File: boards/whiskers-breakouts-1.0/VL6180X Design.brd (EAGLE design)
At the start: 76.5 x 21 mm, 19 parts, among them J2 6-PIN_2MM-V, Q3 BSS138, Q4 BSS138, U1 VL6180X, U2 MIC5225_2.8V, U3 VL6180X, U4 VL6180X

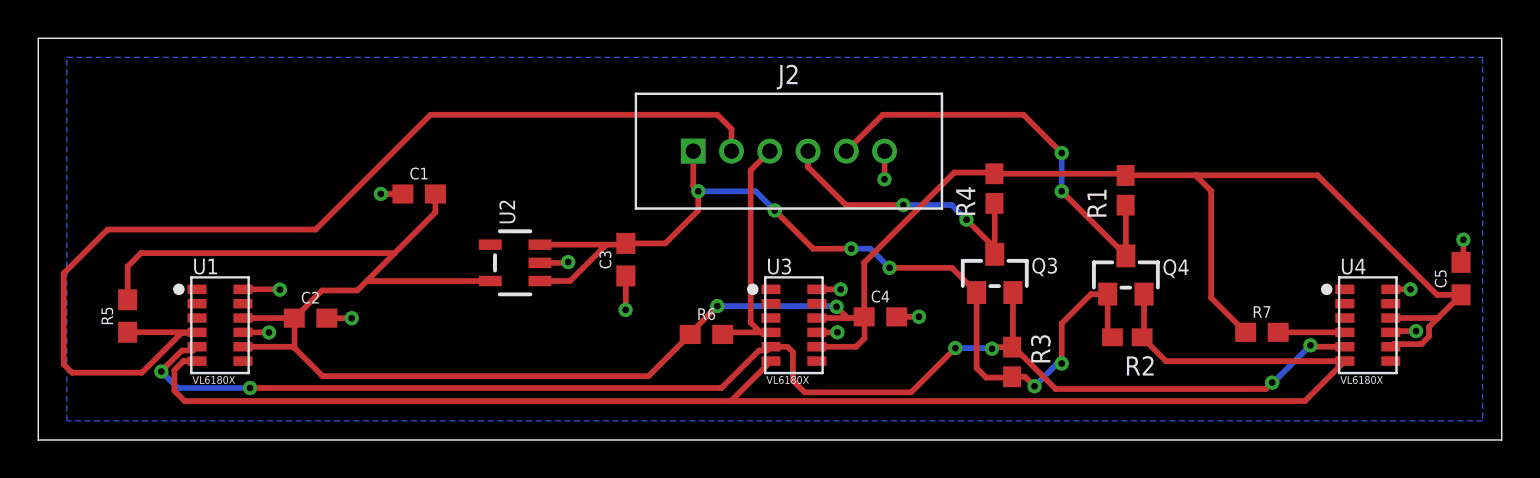
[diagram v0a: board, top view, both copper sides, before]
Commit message: Update VL6180X Design.brd
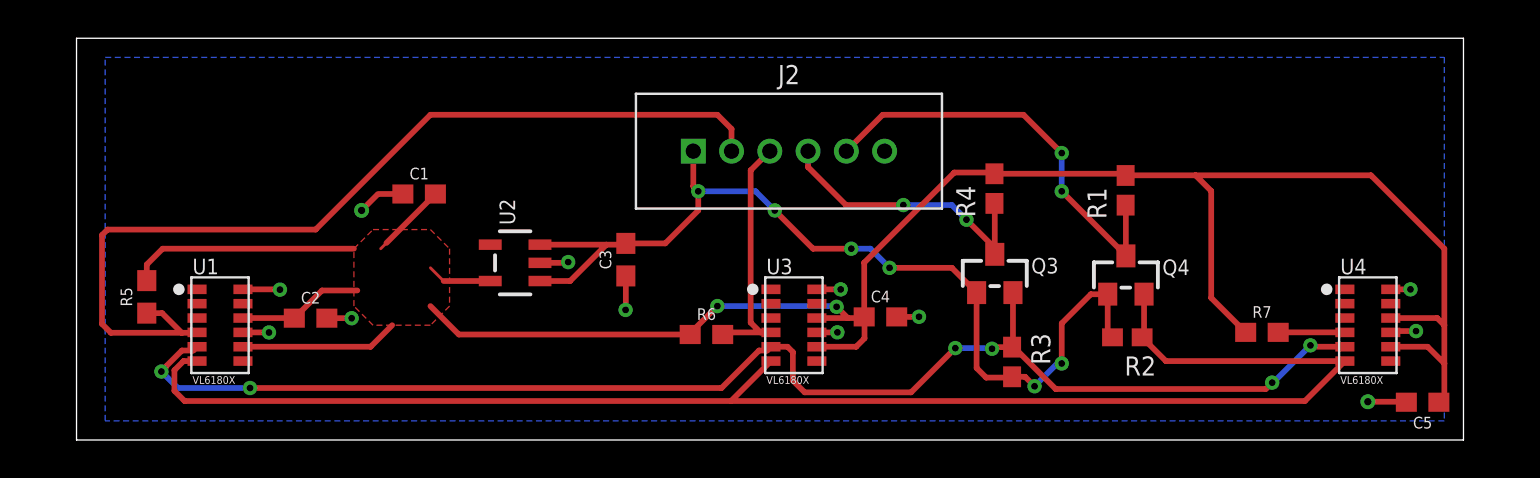
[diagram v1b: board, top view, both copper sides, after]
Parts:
- moved C5 6.77 mm to (72.9, 16.0), turned to 180 degrees
- moved R5 1.41 mm to (6.17, 21.5)
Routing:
- net VCC: track 133.2 -> 124.3 mm
- net RST_1: track 56.2 -> 49.0 mm
- net GND: track 17.6 -> 18.3 mm, vias 13 -> 12
- added copper zone on layer 1, net VCC
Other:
- board size 76.5 x 21 mm -> 72.5 x 21 mm

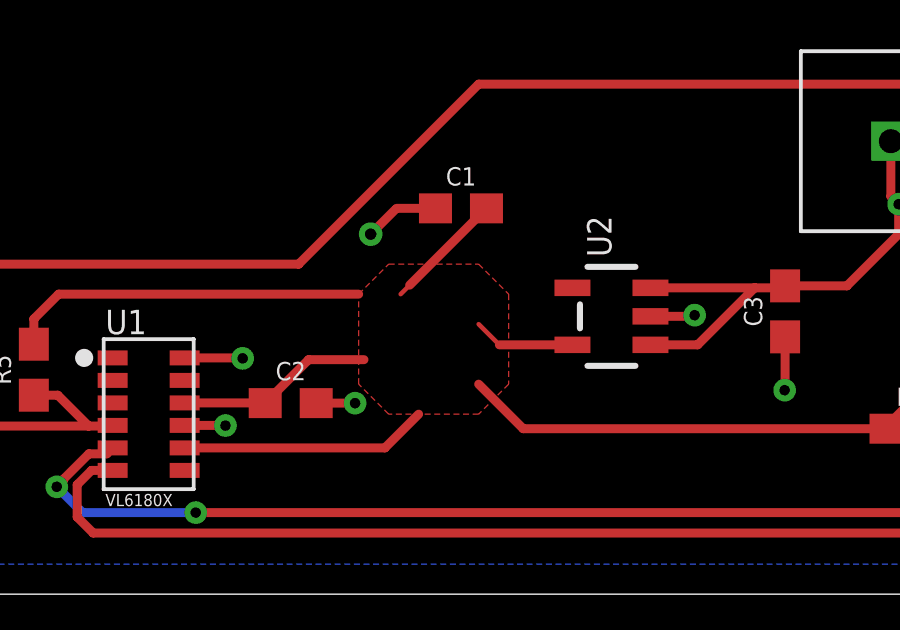
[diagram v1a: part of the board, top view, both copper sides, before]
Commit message: Update VL6180X Design.brd
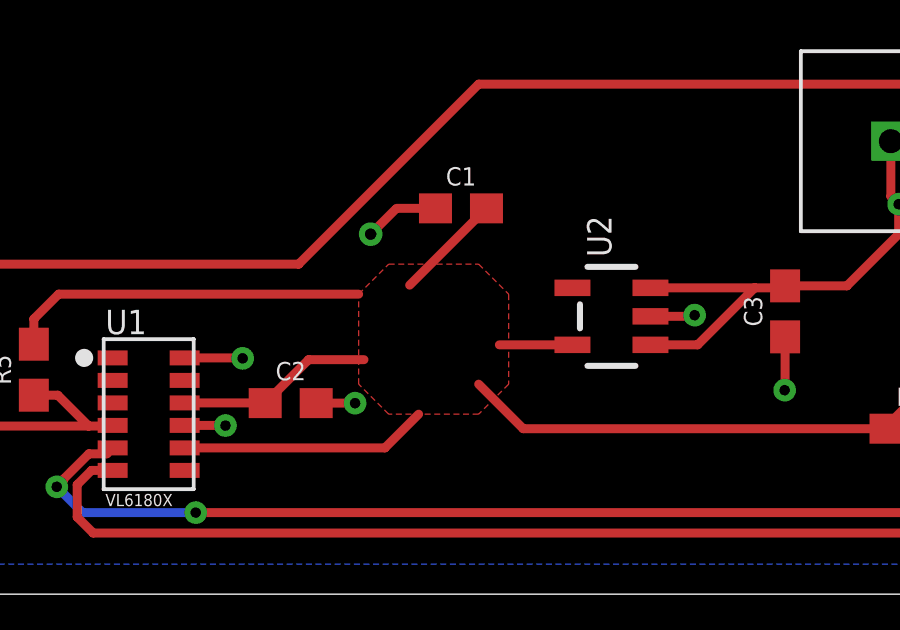
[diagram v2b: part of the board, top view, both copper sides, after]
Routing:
- net VCC: track 124.3 -> 122.9 mm
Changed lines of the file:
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@@
 <vertex x="17" y="24"/>
 </polygon>
-<wire x1="18.4" y1="24" x2="18.7" y2="24.3" width="0.1524" layer="1"/>
 <wire x1="18.7" y1="24.3" x2="21.26" y2="26.86" width="0.3" layer="1"/>
 <wire x1="24.126421875" y1="22.31048125" x2="21.68951875" y2="22.31048125" width="0.3" layer="1"/>
-<wire x1="21.68951875" y1="22.31048125" x2="21" y2="23" width="0.1524" layer="1"/>
 <wire x1="11.2" y1="18.875" x2="17.875" y2="18.875" width="0.3" layer="1"/>
 <wire x1="17.875" y1="18.875" x2="19" y2="20" width="0.3" layer="1"/>

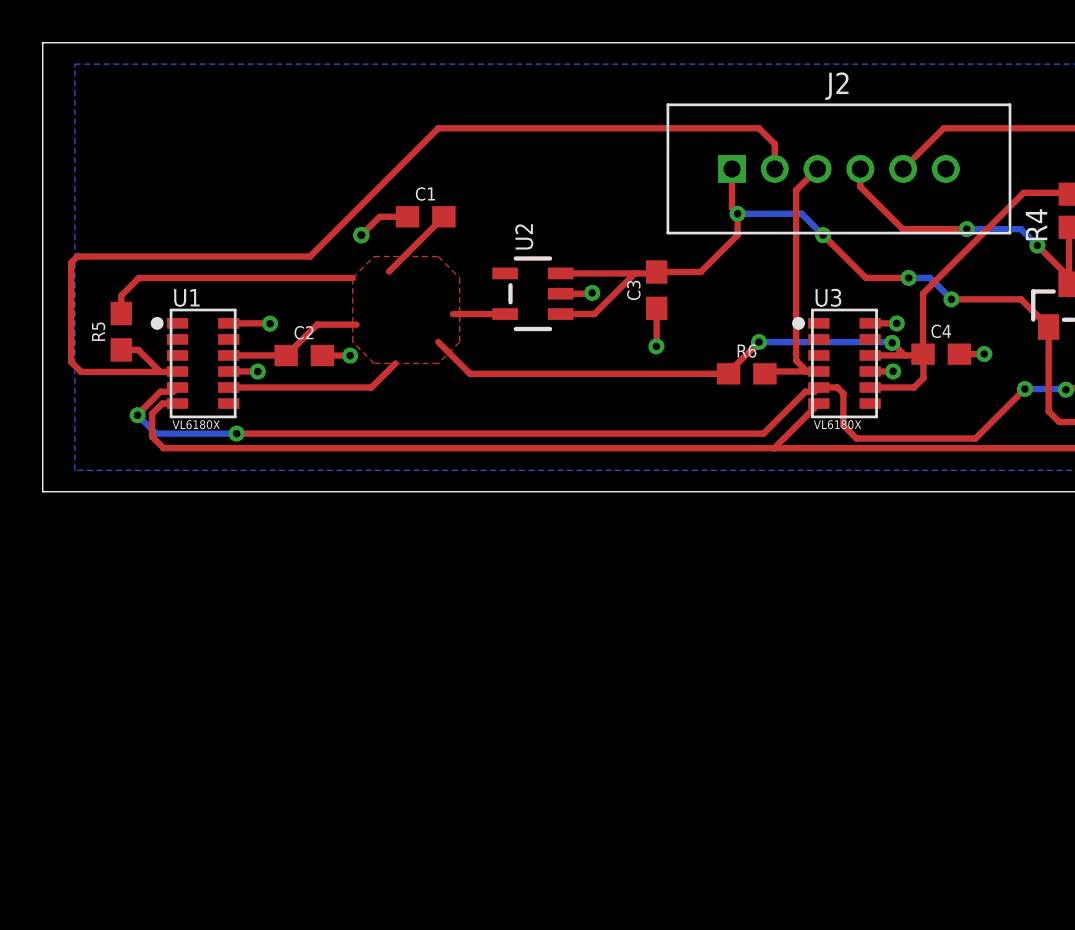
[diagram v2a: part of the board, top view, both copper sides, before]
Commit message: Schematic Correction
Added Capacitors to VL6180X to match typical application schematic found on datasheet. Fixed ports on MOLEX to align with control boards i2c port (swapped SDA and SCL, change 3.3V to 5V). Added additional voltage regulator to step down 5V to 3.3V.
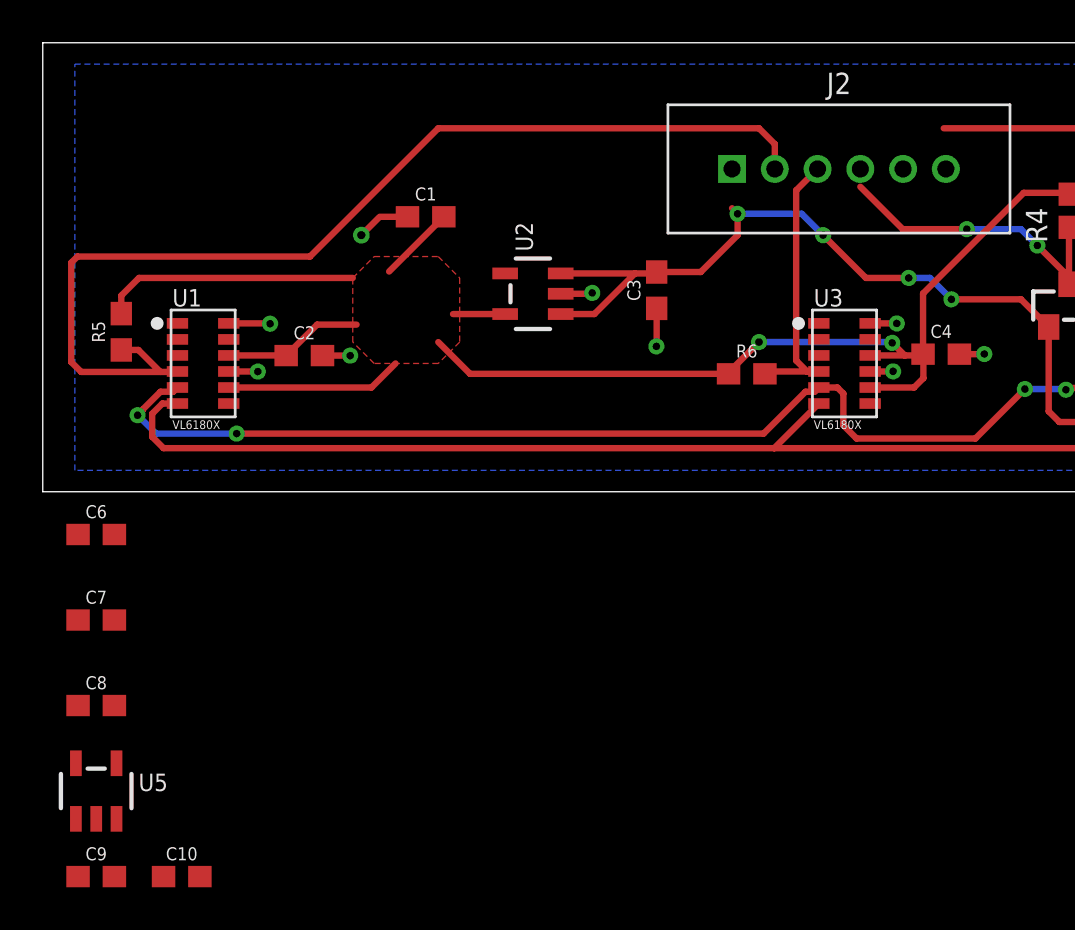
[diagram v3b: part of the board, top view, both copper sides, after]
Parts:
- added C10, C9: 1uF, SparkFun-Capacitors:0603
- added C6, C7, C8: 4.7uF, SparkFun-Capacitors:0603
- added U5: MIC5225_2.8V, microbuilder:SOT23-5
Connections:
- new net +5V: C10.2, J2.1, U5.1, U5.3
- net +3.3V: now also C9.2, U5.5; no longer J2.1
- net GND: now also C10.1, C6.2, C7.2, C8.2, C9.1, U5.2
- net SCL_3.3V: now also J2.5; no longer J2.4
- net SDA_3.3V: now also J2.4; no longer J2.5
- net VCC: now also C6.1, C7.1, C8.1
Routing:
- net SDA_3.3V: track 22.1 -> 19.4 mm
- net +3.3V: track 50.1 -> 48.3 mm
- net SCL_3.3V: track 15.3 -> 14.5 mm
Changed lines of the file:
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@@
 <attribute name="VALUE" x="68.559" y="16.934" size="0.4064" layer="25" ratio="10"/>
+</element>
+<element name="C6" library="SparkFun-Capacitors" library_urn="urn:adsk.eagle:library:510" package="0603" package3d_urn="urn:adsk.eagle:package:37414/1" value="4.7uF" x="5" y="12" smashed="yes">
+<attribute name="NAME" x="5" y="12.762" size="0.6096" layer="25" font="vector" ratio="20" align="bottom-center"/>
+<attribute name="PROD_ID" value="CAP-07886" x="5" y="12" size="1.778" layer="27" display="off"/>
+<attribute name="VALUE" x="5" y="11.238" size="0.6096" layer="27" font="vector" ratio="20" align="top-center"/>
+</element>
+<element name="C7" library="SparkFun-Capacitors" library_urn="urn:adsk.eagle:library:510" package="0603" package3d_urn="urn:adsk.eagle:package:37414/1" value="4.7uF" x="5" y="8" smashed="yes">
+<attribute name="NAME" x="5" y="8.762" size="0.6096" layer="25" font="vector" ratio="20" align="bottom-center"/>
+<attribute name="PROD_ID" value="CAP-07886" x="5" y="8" size="1.778" layer="27" display="off"/>
+<attribute name="VALUE" x="5" y="7.238" size="0.6096" layer="27" font="vector" ratio="20" align="top-center"/>
+</element>
+<element name="C8" library="SparkFun-Capacitors" library_urn="urn:adsk.eagle:library:510" package="0603" package3d_urn="urn:adsk.eagle:package:37414/1" value="4.7uF" x="5" y="4" smashed="yes">
+<attribute name="NAME" x="5" y="4.762" size="0.6096" layer="25" font="vector" ratio="20" align="bottom-center"/>
+<attribute name="PROD_ID" value="CAP-07886" x="5" y="4" size="1.778" layer="27" display="off"/>
+<attribute name="VALUE" x="5" y="3.238" size="0.6096" layer="27" font="vector" ratio="20" align="top-center"/>
+</element>
+<element name="U5" library="microbuilder" package="SOT23-5" value="MIC5225_2.8V" x="5" y="0" smashed="yes">
+<attribute name="NAME" x="6.978" y="0" size="0.8128" layer="25" ratio="18"/>
+<attribute name="VALUE" x="6.978" y="-0.635" size="0.4064" layer="27" ratio="10"/>
+</element>
+<element name="C9" library="SparkFun-Capacitors" library_urn="urn:adsk.eagle:library:510" package="0603" package3d_urn="urn:adsk.eagle:package:37414/1" value="1uF" x="5" y="-4" smashed="yes">
+<attribute name="NAME" x="5" y="-3.238" size="0.6096" layer="25" font="vector" ratio="20" align="bottom-center"/>
+<attribute name="PROD_ID" value="CAP-07886" x="5" y="-4" size="1.778" layer="27" display="off"/>
+<attribute name="VALUE" x="5" y="-4.762" size="0.6096" layer="27" font="vector" ratio="20" align="top-center"/>
+</element>
+<element name="C10" library="SparkFun-Capacitors" library_urn="urn:adsk.eagle:library:510" package="0603" package3d_urn="urn:adsk.eagle:package:37414/1" value="1uF" x="9" y="-4" smashed="yes">
+<attribute name="NAME" x="9" y="-3.238" size="0.6096" layer="25" font="vector" ratio="20" align="bottom-center"/>
+<attribute name="PROD_ID" value="CAP-07886" x="5" y="-8" size="1.778" layer="27" display="off"/>
+<attribute name="VALUE" x="9" y="-4.762" size="0.6096" layer="27" font="vector" ratio="20" align="top-center"/>
 </element>
 </elements>
@@
 <wire x1="71.9883" y1="16" x2="70" y2="16" width="0.3" layer="1"/>
 <via x="70" y="16" extent="1-16" drill="0.381"/>
+<contactref element="C7" pad="2"/>
+<contactref element="C8" pad="2"/>
+<contactref element="C6" pad="2"/>
+<contactref element="U5" pad="2"/>
+<contactref element="C10" pad="1"/>
+<contactref element="C9" pad="1"/>
+<wire x1="72.52018125" y1="19.6944" x2="72.22998125" y2="21.87448125" width="0" layer="19" extent="1-1"/>
+<wire x1="72.014178125" y1="15.974121875" x2="71.2" y2="19.625" width="0" layer="19" extent="1-1"/>
+<wire x1="46.53788125" y1="20.44191875" x2="70" y2="16" width="0" layer="19" extent="1-1"/>
+<wire x1="42.27321875" y1="19.62911875" x2="45.373659375" y2="20.4343" width="0" layer="19" extent="1-1"/>
+<wire x1="41.2" y1="21.875" x2="41.2" y2="19.625" width="0" layer="19" extent="1-1"/>
+<wire x1="44.740078125" y1="29.098240625" x2="42.445940625" y2="21.871940625" width="0" layer="19" extent="1-1"/>
+<wire x1="31.2141" y1="22.5768375" x2="41.2" y2="21.875" width="0" layer="19" extent="1-1"/>
+<wire x1="28.2" y1="23.3" x2="31.2141" y2="22.5768375" width="0" layer="19" extent="1-1"/>
+<wire x1="19.56" y1="26.86" x2="26.726621875" y2="23.26048125" width="0" layer="19" extent="1-1"/>
+<wire x1="16.880840625" y1="20.36571875" x2="17.4" y2="26" width="0" layer="19" extent="1-1"/>
+<wire x1="13.13358125" y1="21.859240625" x2="15.584540625" y2="20.368259375" width="0" layer="19" extent="1-1"/>
+<wire x1="11.2" y1="19.625" x2="11.2" y2="21.875" width="0" layer="19" extent="1-1"/>
+<wire x1="5.85" y1="12" x2="11.2" y2="19.625" width="0" layer="19" extent="1-1"/>
+<wire x1="5.85" y1="8" x2="5.85" y2="12" width="0" layer="19" extent="1-1"/>
+<wire x1="5.85" y1="4" x2="5.85" y2="8" width="0" layer="19" extent="1-1"/>
+<wire x1="5" y1="-1.3001" x2="5.85" y2="4" width="0" layer="19" extent="1-1"/>
+<wire x1="4.15" y1="-4" x2="5" y2="-1.3001" width="0" layer="19" extent="1-1"/>
+<wire x1="8.15" y1="-4" x2="4.15" y2="-4" width="0" layer="19" extent="1-1"/>
 </signal>
 <signal name="+3.3V">
@@
 <contactref element="U2" pad="3"/>
 <contactref element="C3" pad="2"/>
-<contactref element="J2" pad="1"/>
 <wire x1="56.4032" y1="21.62378125" x2="56.4032" y2="21.562059375" width="0.3" layer="1"/>
 <wire x1="49.55028125" y1="21.705059375" x2="49.55028125" y2="17.762259375" width="0.3" layer="1"/>
@@
 <wire x1="55.521859375" y1="21.617940625" x2="56.34731875" y2="21.617940625" width="0.3" layer="1"/>
 <wire x1="56.34731875" y1="21.617940625" x2="56.4032" y2="21.562059375" width="0.3" layer="1"/>
-<wire x1="34.740078125" y1="27.259921875" x2="34.740078125" y2="29.098240625" width="0.3" layer="1"/>
 <wire x1="34.740078125" y1="27.259921875" x2="35" y2="27" width="0.3" layer="1"/>
 <via x="35" y="27" extent="1-16" drill="0.35"/>
@@
 <wire x1="56.4032" y1="21.62378125" x2="56.4032" y2="19.61738125" width="0.3" layer="1"/>
 <wire x1="56.4032" y1="19.61738125" x2="56.65241875" y2="19.3681625" width="0.3" layer="1"/>
+<contactref element="U5" pad="5"/>
+<contactref element="C9" pad="2"/>
+<wire x1="4.05" y1="1.3001" x2="26.726621875" y2="22.31048125" width="0" layer="19" extent="1-1"/>
+<wire x1="5.85" y1="-4" x2="4.05" y2="1.3001" width="0" layer="19" extent="1-1"/>
 </signal>
 <signal name="SCL_3.3V">
 <contactref element="Q3" pad="3"/>
 <contactref element="R4" pad="1"/>
-<contactref element="J2" pad="4"/>
 <wire x1="50.50028125" y1="26.34965625" x2="50.50028125" y2="23.705059375" width="0.3" layer="1"/>
 <wire x1="50.50028125" y1="26.34965625" x2="50.4825" y2="26.3674375" width="0.3" layer="1"/>
-<wire x1="40.740078125" y1="29.098240625" x2="40.740078125" y2="28.2641" width="0.3" layer="1"/>
 <wire x1="42.723559375" y1="26.28061875" x2="45.71938125" y2="26.28061875" width="0.3" layer="1"/>
 <via x="45.71938125" y="26.28061875" extent="1-16" drill="0.35"/>
@@
 <wire x1="50.50028125" y1="24.03601875" x2="50.50028125" y2="23.705059375" width="0.3" layer="1"/>
 <wire x1="40.740078125" y1="28.2641" x2="42.723559375" y2="26.28061875" width="0.3" layer="1"/>
+<contactref element="J2" pad="5"/>
+<wire x1="40.740078125" y1="28.2641" x2="42.740078125" y2="29.098240625" width="0" layer="19" extent="1-1"/>
 </signal>
 <signal name="RST_1">
@@
 <contactref element="Q4" pad="3"/>
 <contactref element="R1" pad="1"/>
-<contactref element="J2" pad="5"/>
 <wire x1="57.3532" y1="23.62378125" x2="57.3532" y2="24" width="0.3" layer="1"/>
 <wire x1="57.3532" y1="24" x2="57.3532" y2="26.2639625" width="0.3" layer="1"/>
 <wire x1="57.3532" y1="26.2639625" x2="57.33998125" y2="26.27718125" width="0.3" layer="1"/>
-<wire x1="42.740078125" y1="29.098240625" x2="44.6418375" y2="31" width="0.3" layer="1"/>
 <wire x1="52" y1="31" x2="54" y2="29" width="0.3" layer="1"/>
 <via x="54" y="29" extent="1-16" drill="0.35"/>
@@
 <wire x1="57" y1="24" x2="57.3532" y2="24" width="0.3" layer="1"/>
 <wire x1="44.6418375" y1="31" x2="52" y2="31" width="0.3" layer="1"/>
+<contactref element="J2" pad="4"/>
+<wire x1="40.740078125" y1="29.098240625" x2="44.6418375" y2="31" width="0" layer="19" extent="1-1"/>
 </signal>
 <signal name="VCC">
@@
 <wire x1="6.173221875" y1="23.173221875" x2="7" y2="24" width="0.3" layer="1"/>
 <wire x1="7" y1="24" x2="17" y2="24" width="0.3" layer="1"/>
+<contactref element="C7" pad="1"/>
+<contactref element="C8" pad="1"/>
+<contactref element="C6" pad="1"/>
+<wire x1="17" y1="24" x2="18.7" y2="24.3" width="0" layer="19" extent="1-1"/>
+<wire x1="17.17801875" y1="21.816059375" x2="17" y2="24" width="0" layer="19" extent="1-1"/>
+<wire x1="11.2" y1="18.875" x2="11.2" y2="20.375" width="0" layer="19" extent="1-1"/>
+<wire x1="21" y1="21" x2="19" y2="20" width="0" layer="19" extent="1-1"/>
+<wire x1="21.68951875" y1="22.31048125" x2="21" y2="21" width="0" layer="19" extent="1-1"/>
+<wire x1="4.15" y1="12" x2="11.2" y2="18.875" width="0" layer="19" extent="1-1"/>
+<wire x1="4.15" y1="8" x2="4.15" y2="12" width="0" layer="19" extent="1-1"/>
+<wire x1="4.15" y1="4" x2="4.15" y2="8" width="0" layer="19" extent="1-1"/>
 </signal>
 <signal name="RST_2">
@@
 <wire x1="40.56351875" y1="16.4899625" x2="46.12414375" y2="16.4899625" width="0.3" layer="1"/>
 </signal>
+<signal name="+5V">
+<contactref element="J2" pad="1"/>
+<contactref element="U5" pad="1"/>
+<contactref element="U5" pad="3"/>
+<contactref element="C10" pad="2"/>
+<wire x1="9.85" y1="-4" x2="34.740078125" y2="29.098240625" width="0" layer="19" extent="1-1"/>
+<wire x1="5.95" y1="-1.3001" x2="9.85" y2="-4" width="0" layer="19" extent="1-1"/>
+<wire x1="4.05" y1="-1.3001" x2="5.95" y2="-1.3001" width="0" layer="19" extent="1-1"/>
+</signal>
 </signals>

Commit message: Naming Components
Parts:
- U2: value MIC5225_2.8V -> TLV74128PDBVR
- U5: value MIC5225_2.8V -> MIC5225-3.3YM5-TR
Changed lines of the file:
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@@
 <attribute name="VALUE" x="8.559" y="16.934" size="0.4064" layer="25" ratio="10"/>
 </element>
-<element name="U2" library="microbuilder" package="SOT23-5" value="MIC5225_2.8V" x="25.426521875" y="23.26048125" smashed="yes" rot="R90">
+<element name="U2" library="microbuilder" package="SOT23-5" value="TLV74128PDBVR" x="25.426521875" y="23.26048125" smashed="yes" rot="R90">
 <attribute name="NAME" x="25.426521875" y="25.23848125" size="0.8128" layer="25" ratio="18" rot="R90"/>
 <attribute name="VALUE" x="26.061521875" y="25.23848125" size="0.4064" layer="27" ratio="10" rot="R90"/>
@@
 <attribute name="VALUE" x="5" y="3.238" size="0.6096" layer="27" font="vector" ratio="20" align="top-center"/>
 </element>
-<element name="U5" library="microbuilder" package="SOT23-5" value="MIC5225_2.8V" x="5" y="0" smashed="yes">
+<element name="U5" library="microbuilder" package="SOT23-5" value="MIC5225-3.3YM5-TR" x="5" y="0" smashed="yes">
 <attribute name="NAME" x="6.978" y="0" size="0.8128" layer="25" ratio="18"/>
 <attribute name="VALUE" x="6.978" y="-0.635" size="0.4064" layer="27" ratio="10"/>
